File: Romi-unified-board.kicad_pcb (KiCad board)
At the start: 4 copper layers, 125.1 x 125.8 mm, 68 parts, among them J1 ServoAnalog, J10 LIDAR_DATA, J11 LIDAR_MOTOR, J12 ROMI-Encoder, J13 ROMI-Encoder, J14 THING, J15 THING, J2 Conn_01x19_Female, J3 LineSensor, J4 LineSensor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

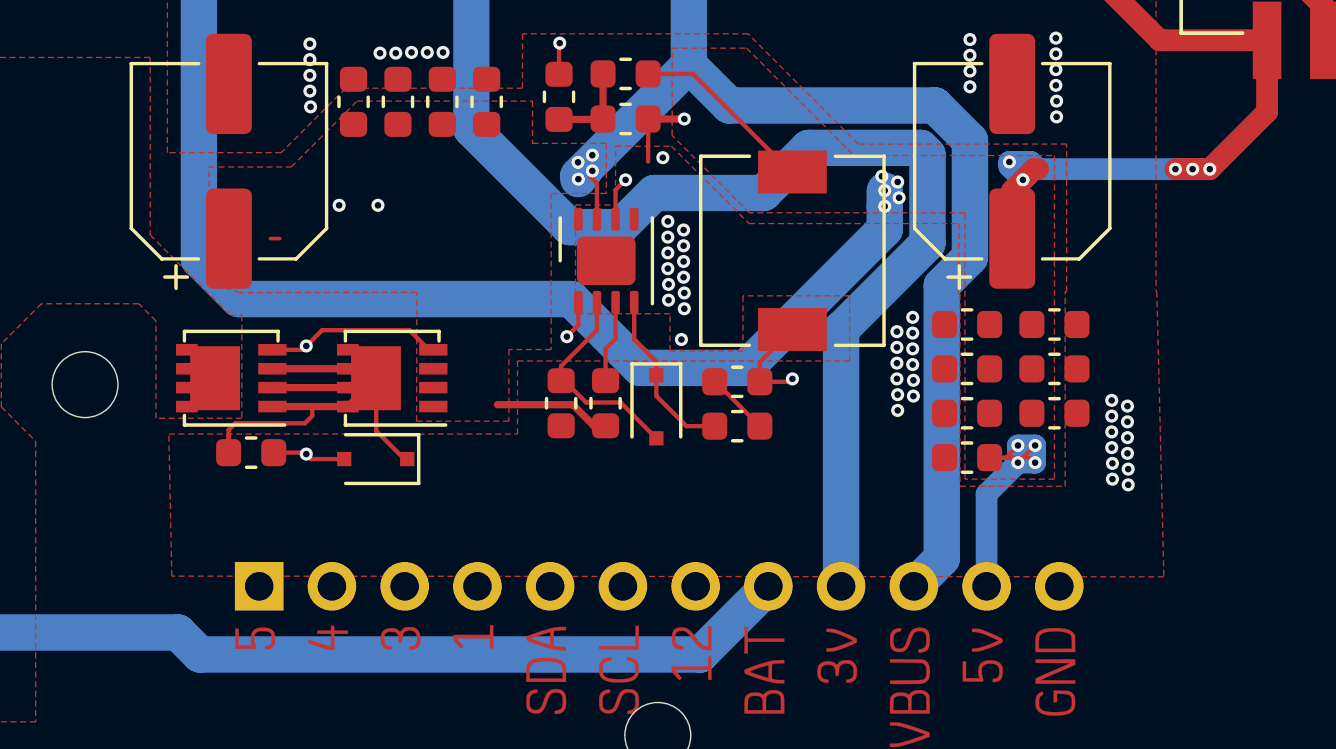
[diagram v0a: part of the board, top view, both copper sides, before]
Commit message: Changes for rev2
rotated Q2
Fixed too-thin trace in DC-DC Circuit.
Created correct footprint for U1. No 9th pad.
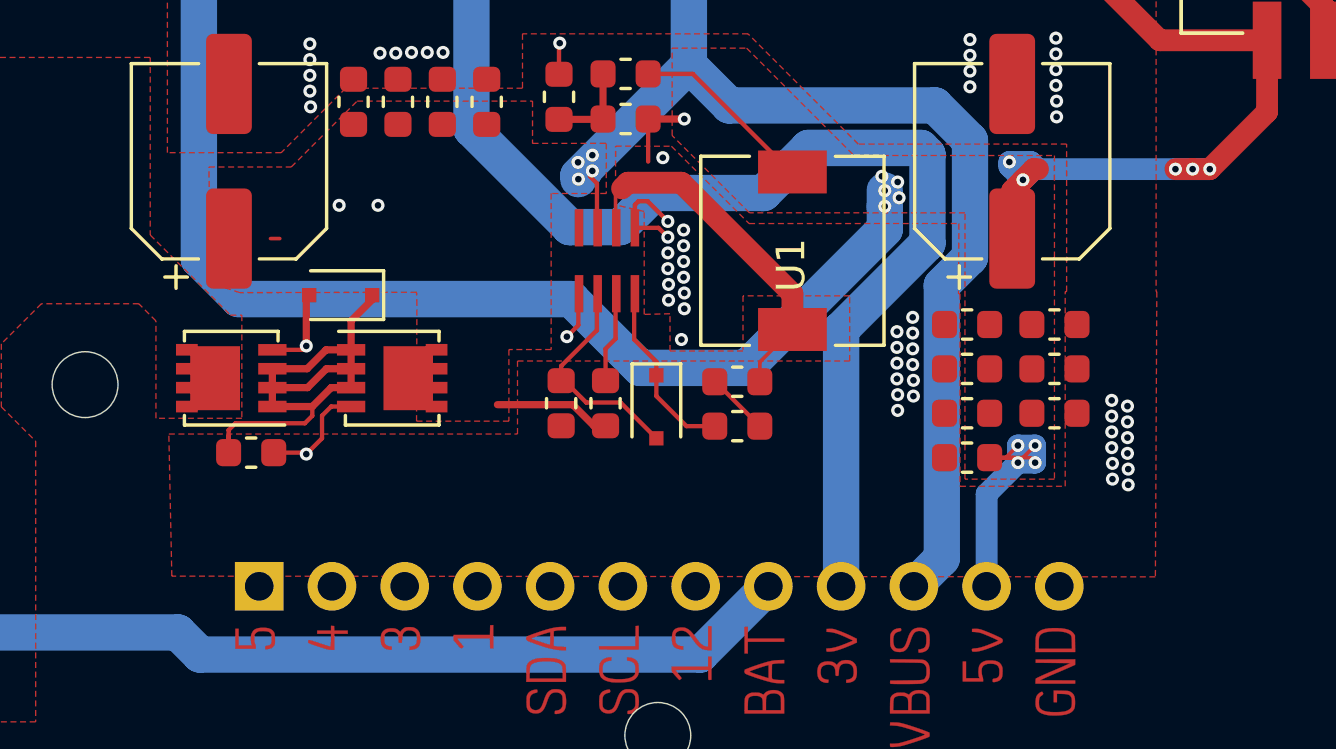
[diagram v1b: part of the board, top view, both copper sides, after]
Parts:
- U1: footprint Package_DFN_QFN:DFN-8-1EP_3x3mm_P0.65mm_EP1.7x2.05mm -> unified:MP4423H
- moved D3 5.85 mm to (82.8, 136.9)
- turned Q2 to 0 degrees
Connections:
- Q2 pad 1: VBUS -> Net-(D3-Pad1)
- Q2 pad 2: VBUS -> Net-(D3-Pad1)
- Q2 pad 3: VBUS -> Net-(D3-Pad1)
- Q2 pad 5: Net-(D3-Pad1) -> VBUS
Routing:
- net GND: track 20.2 -> 23.8 mm
- net Net-(C7-Pad2): track 14.9 -> 12.4 mm, vias 2 -> 0
- net Net-(D3-Pad2): track 111.9 -> 110.1 mm
- net Net-(D3-Pad1): track 19.7 -> 18.8 mm

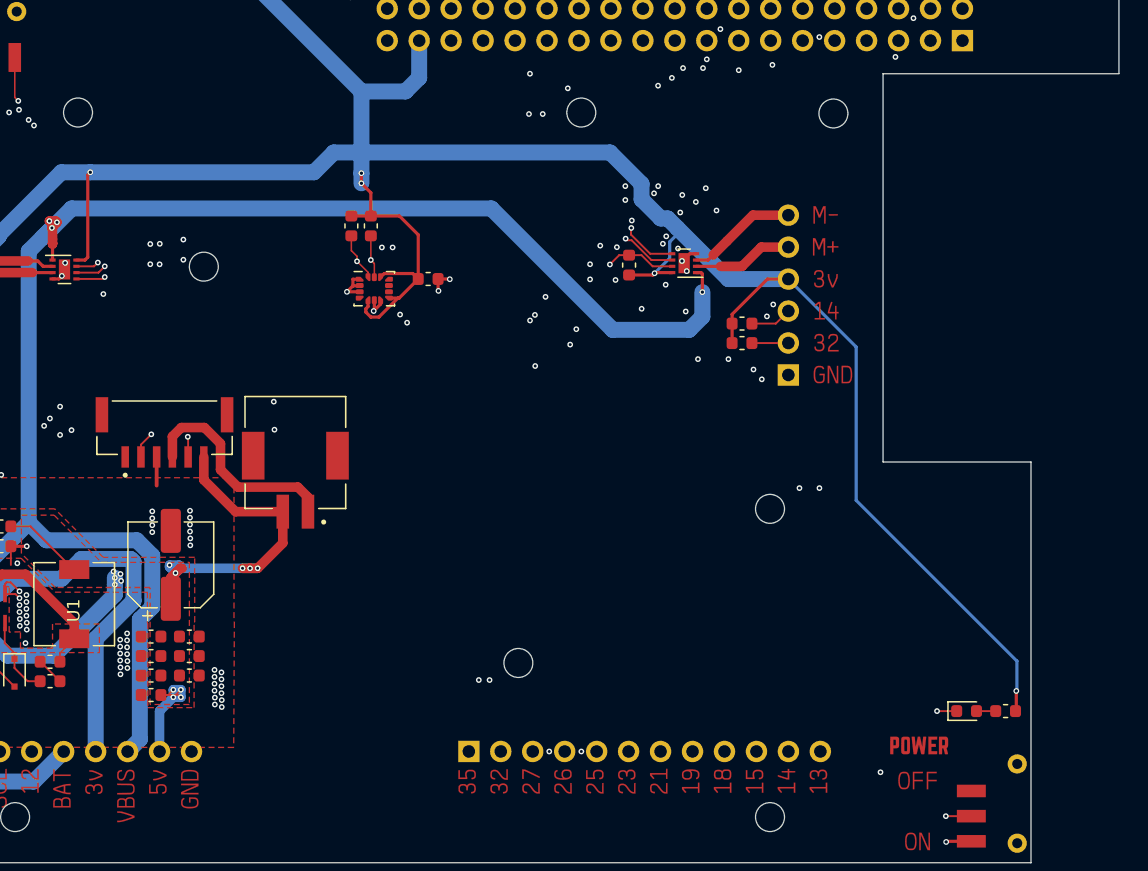
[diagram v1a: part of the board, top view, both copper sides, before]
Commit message: Motor Disable is now a physical switch.
#7
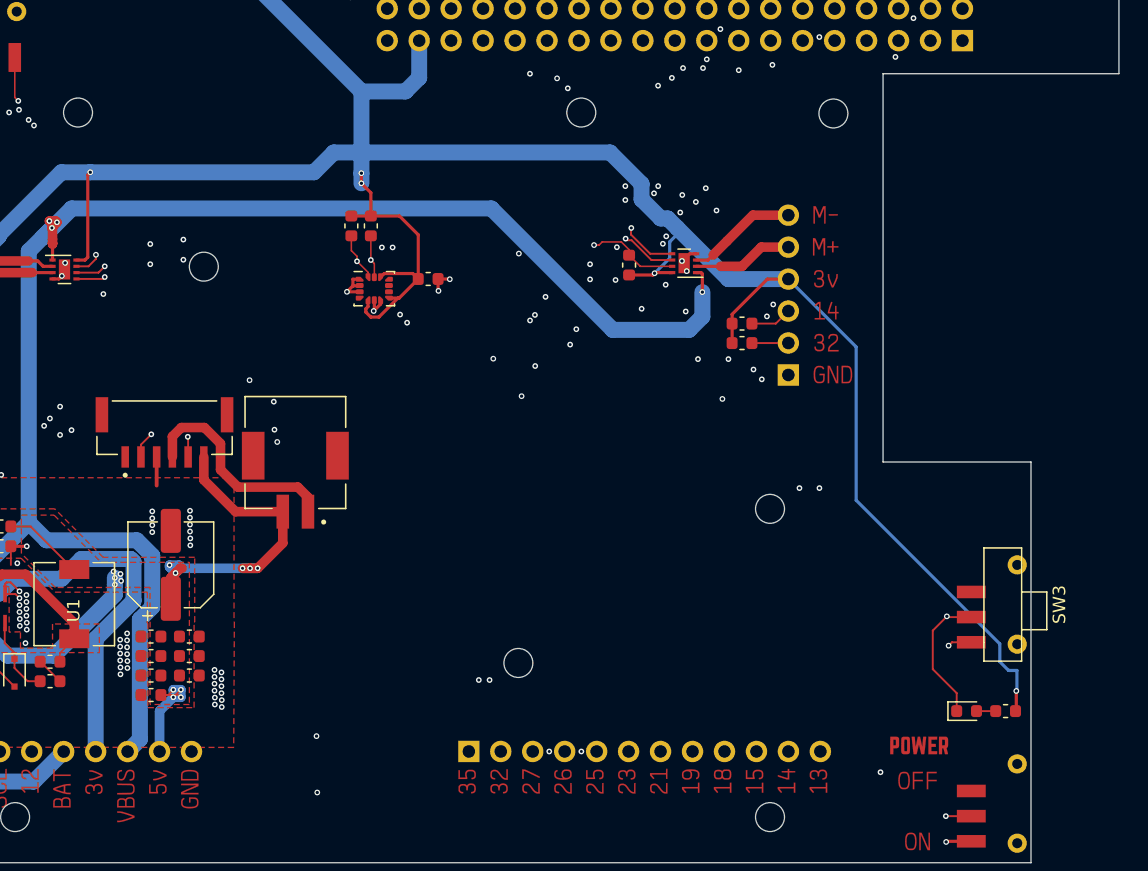
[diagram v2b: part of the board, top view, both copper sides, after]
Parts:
- added SW3: SW_SPST, unified:CSS-1210TB, F.Cu at (169.9, 135.4)
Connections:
- D8 pad 1: GPIO15 -> MOTOR_DISABLE
- R8 pad 2: GPIO15 -> MOTOR_DISABLE
- U2 pad 7: GPIO15 -> MOTOR_DISABLE
- U3 pad 7: GPIO15 -> MOTOR_DISABLE
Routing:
- net MOTOR_DISABLE: track 0.00 -> 189.1 mm, vias 0 -> 8
- net GPIO15: track 180.6 -> 122.5 mm, vias 10 -> 4
- net GND: track 23.8 -> 25.7 mm, vias 69 -> 70

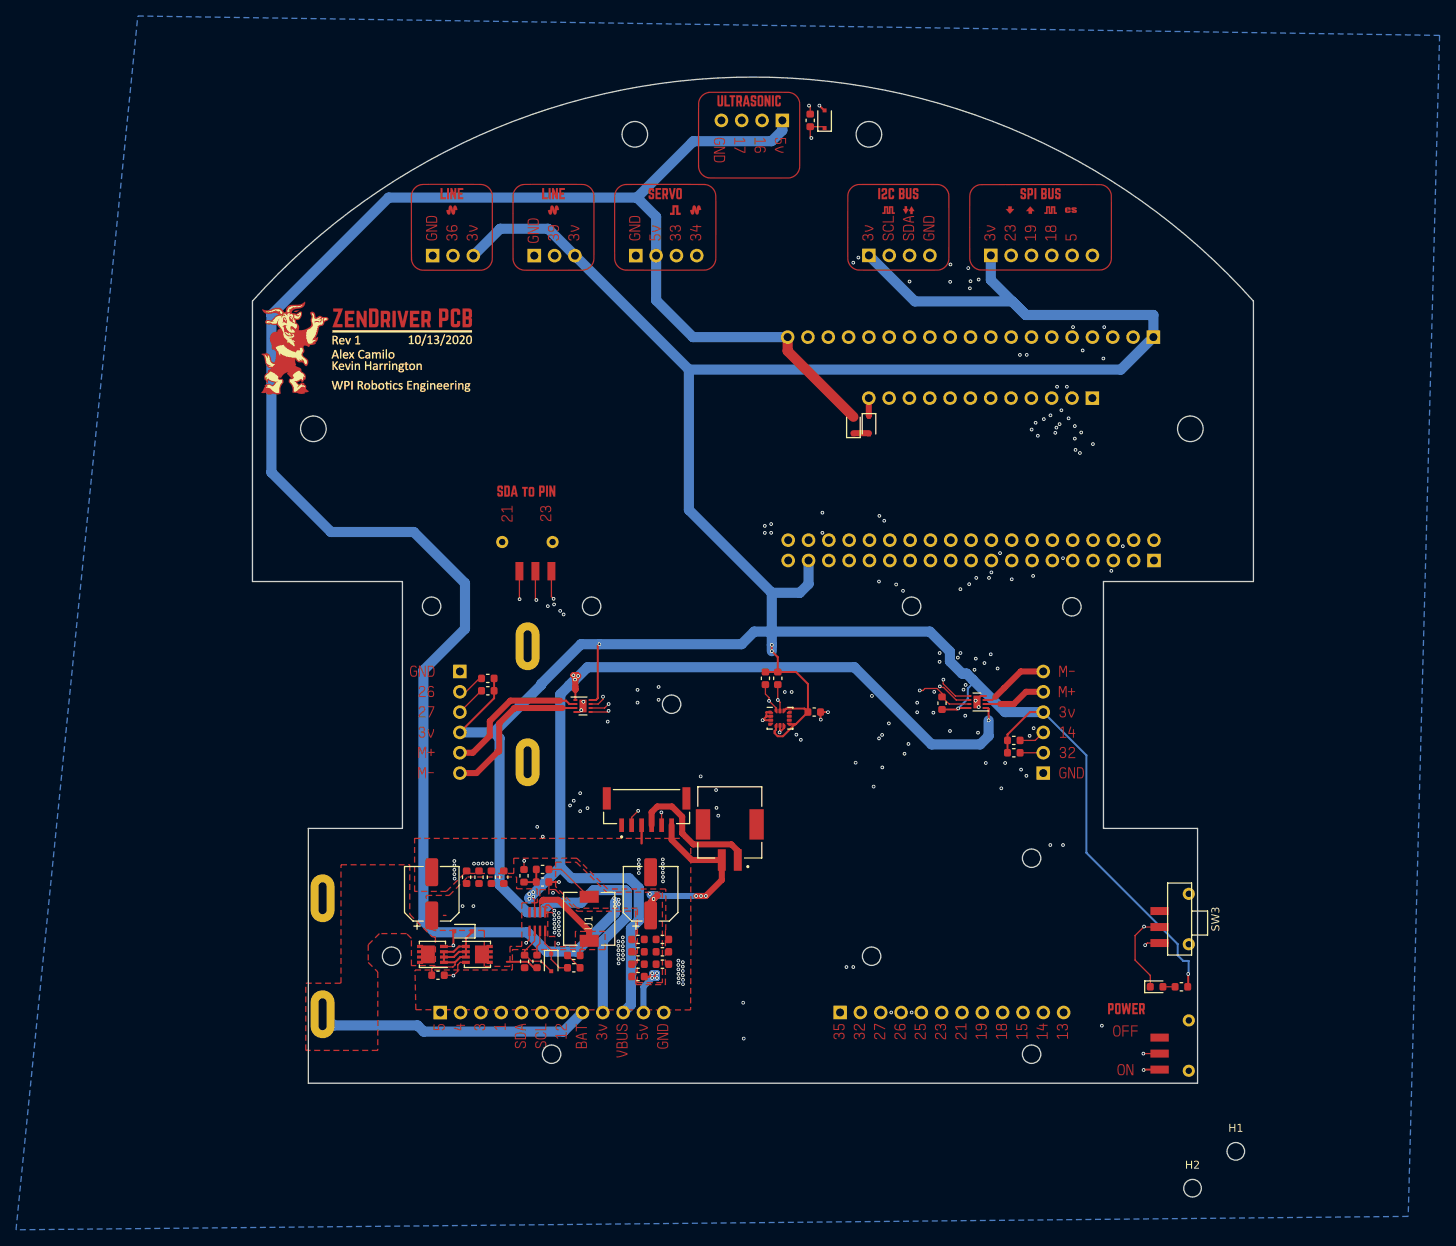
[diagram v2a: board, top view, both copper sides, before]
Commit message: Rev2
Added smart servo connectors
Added IR sensor
Updated silk label
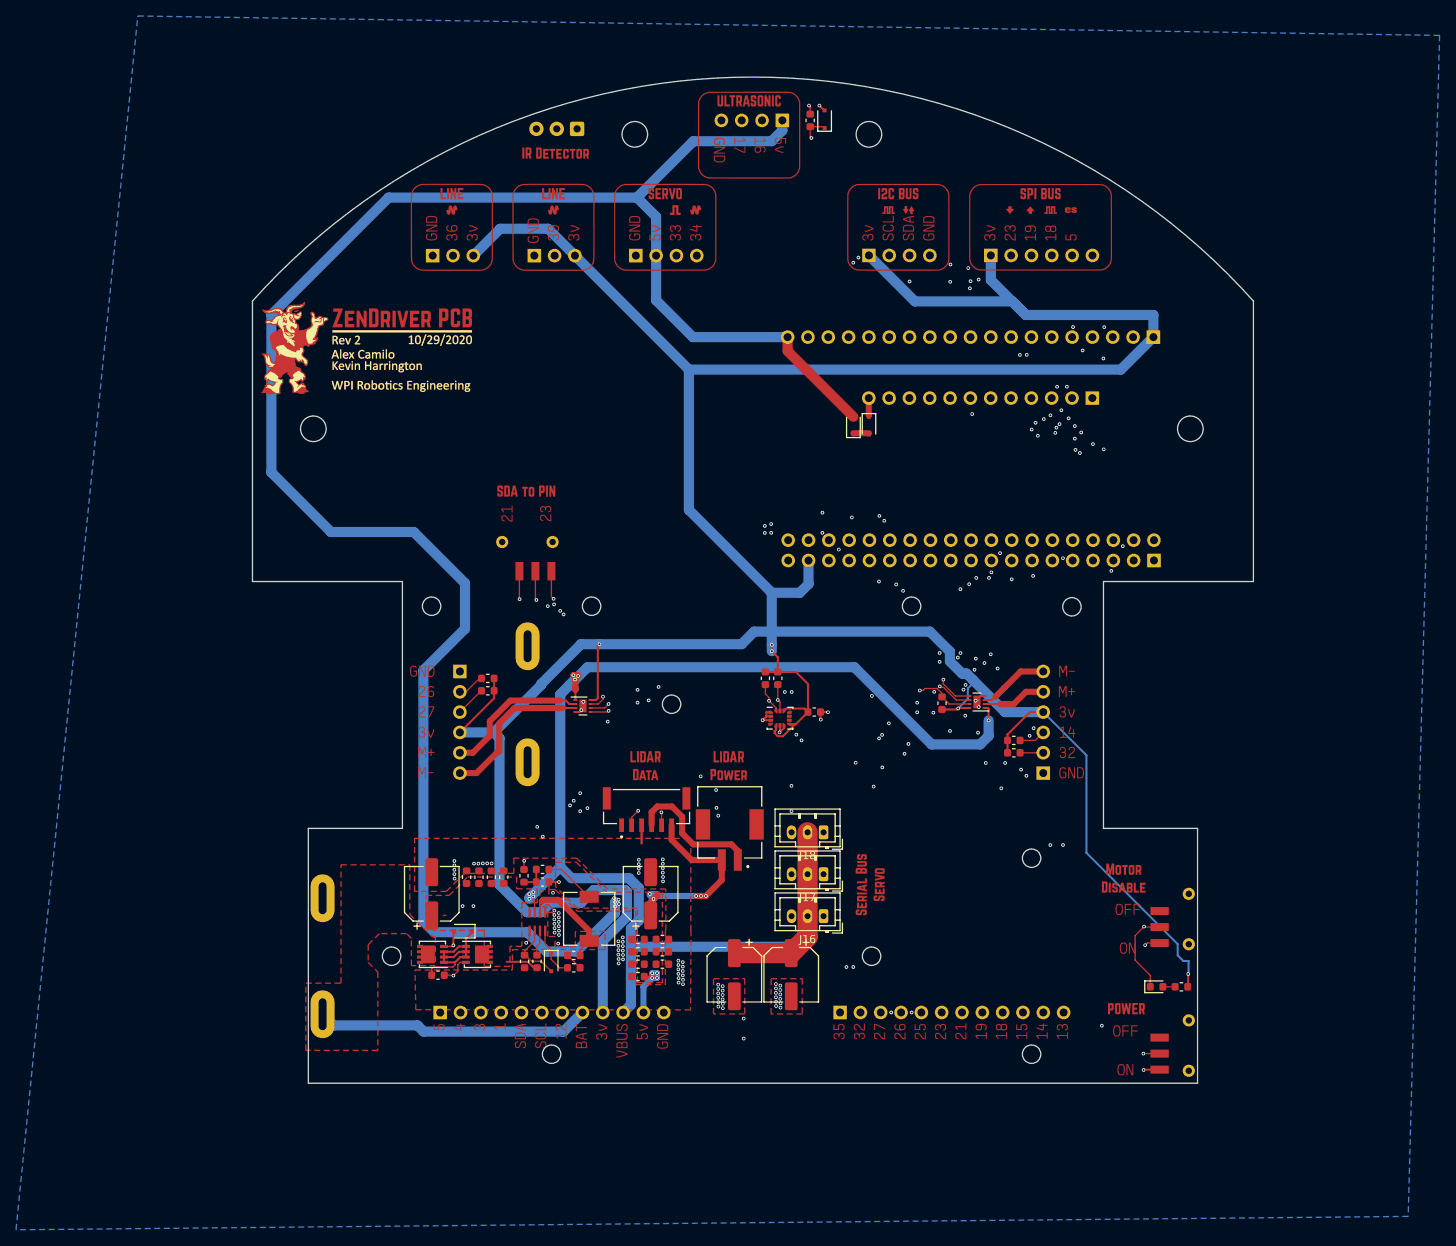
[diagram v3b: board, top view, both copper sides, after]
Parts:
- removed H1, H2: MountingHole, MountingHole:MountingHole_2.2mm_M2_DIN965
- added C16: 220u, Capacitor_SMD:CP_Elec_6.3x3.9, F.Cu at (116.8, 142.3)
- added C17: 220u, Capacitor_SMD:CP_Elec_6.3x3.9, F.Cu at (123.9, 142.3)
- added J16: Conn_01x03_Male, Connector_JST:JST_PH_B3B-PH-K_1x03_P2.00mm_Vertical, F.Cu at (127.9, 135.0)
- added J17: Conn_01x03_Male, Connector_JST:JST_PH_B3B-PH-K_1x03_P2.00mm_Vertical, F.Cu at (127.9, 129.8)
- added J18: Conn_01x03_Male, Connector_JST:JST_PH_B3B-PH-K_1x03_P2.00mm_Vertical, F.Cu at (127.9, 124.5)
- added U4: TSSP58038, OptoDevice:Vishay_MINICAST-3Pin, F.Cu at (97.1, 36.6)
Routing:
- net GPIO15: track 122.5 -> 249.4 mm, vias 4 -> 5
- net GPIO33: track 58.4 -> 143.0 mm, vias 2 -> 7
- net VBUS: track 131.1 -> 188.2 mm
- net +3V3: track 429.1 -> 448.9 mm
- net GPIO27: track 165.9 -> 175.0 mm
- net MOTOR_DISABLE: track 189.1 -> 189.9 mm
- net GPIO12: track 115.2 -> 114.5 mm
- net GND: vias 70 -> 94

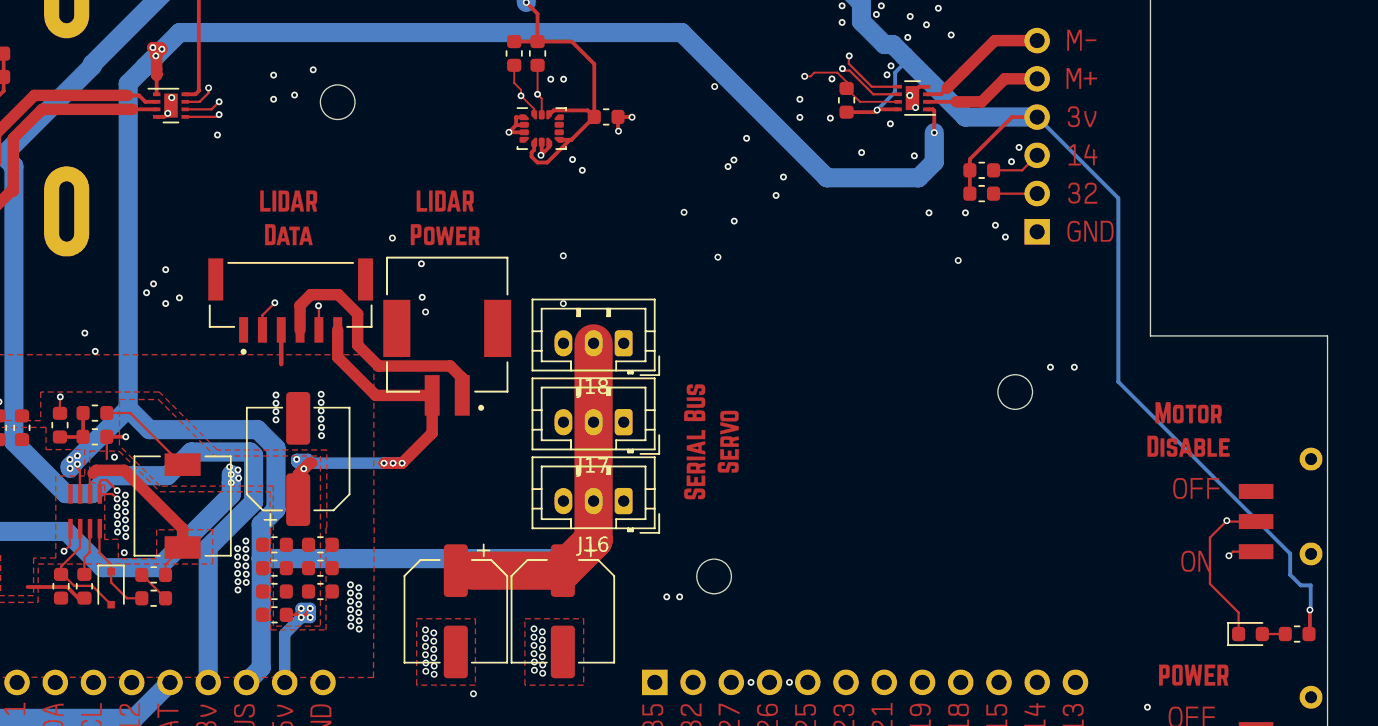
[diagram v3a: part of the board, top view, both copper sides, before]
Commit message: More rev2 changes
Fixed inductor FP
Swapped out accelerometer with an in stock variant.
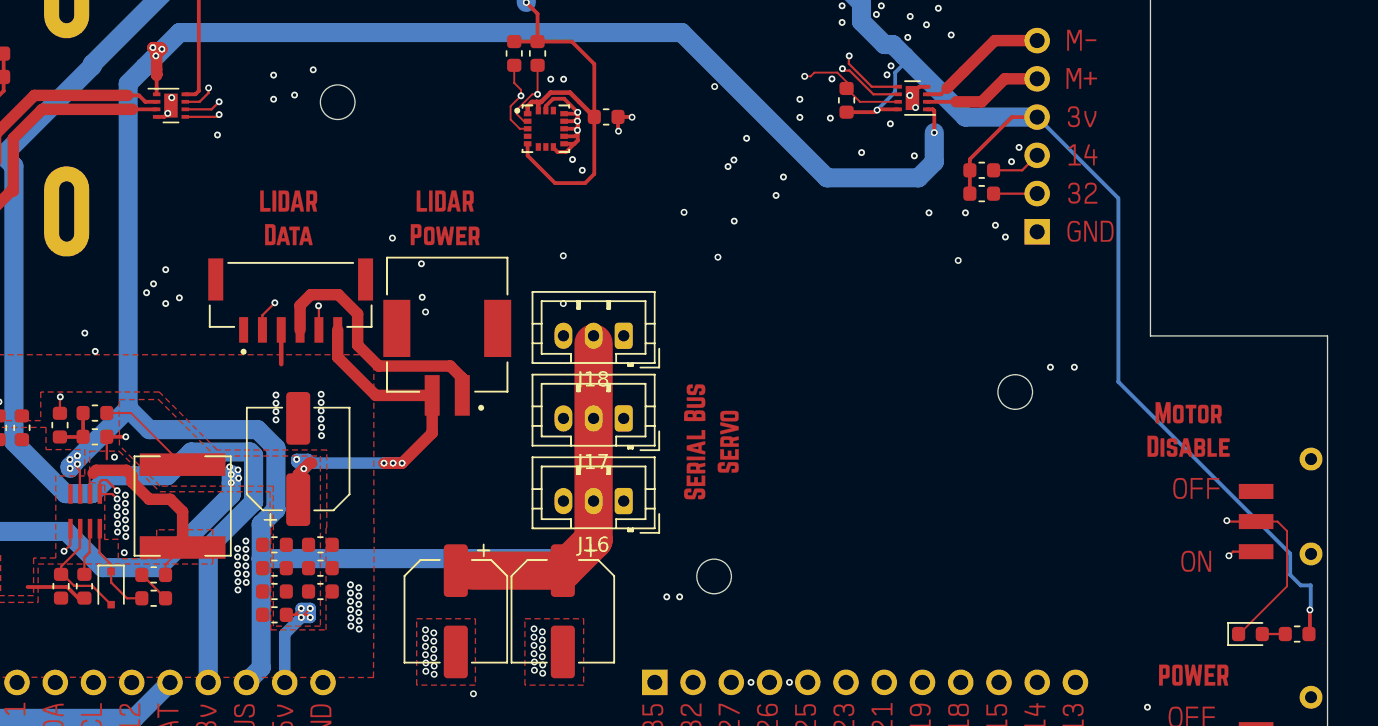
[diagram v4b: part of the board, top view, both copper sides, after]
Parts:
- removed U9: LSM6DS3, Package_LGA:LGA-14_3x2.5mm_P0.5mm_LayoutBorder3x4y
- added U5: LSM6DS33TR, unified:PQFN50P300X300X86-16N, F.Cu at (122.8, 110.3)
- moved J18 0.50 mm to (127.9, 124.0)
- moved J17 0.25 mm to (127.9, 129.5)
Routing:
- net GND: track 25.7 -> 32.8 mm, vias 94 -> 95
- net +3V3: track 448.9 -> 455.4 mm
- net MOTOR_DISABLE: track 189.9 -> 191.7 mm
- net SDA: track 171.1 -> 172.7 mm
- net GPIO22: track 201.9 -> 203.4 mm
- net Net-(C7-Pad2): track 12.4 -> 13.3 mm
